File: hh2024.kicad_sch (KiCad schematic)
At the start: 68 parts, among them J1 SAO, J2 QWIIC, J3 Micro_SD_Card, J4 USB-C, K1 SANYOU_SRD_Form_C, Q3 AP2302B, SW1 Multi-Directional-Switches, SW2 Multi-Directional-Switches, SW3 Multi-Directional-Switches, SW4 Multi-Directional-Switches, SW5 Multi-Directional-Switches, U5 CH32V003F4U6, U6 74LVC1G125

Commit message: Fixed the sao ヽ༼ ツ ༽ﾉ
and some routing
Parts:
- J1: footprint BamboulabFootprints:SAO2 -> BamboulabFootprints:SAO Female THT Labels
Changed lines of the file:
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@@
       (effects (font (size 1.27 1.27)) (justify left))
     )
-    (property "Footprint" "BamboulabFootprints:SAO2" (at 149.86 39.37 0)
+    (property "Footprint" "BamboulabFootprints:SAO Female THT Labels" (at 149.86 39.37 0)
       (effects (font (size 1.27 1.27)) hide)
     )

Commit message: Small fixes and change footprint library for missing libraries
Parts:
- removed TP11, TP12, TP13, TP14, TP15, TP16, TP17: TestPoint, TestPoint:TestPoint_Pad_1.0x1.0mm, symbol Connector:TestPoint
- D10, D11, D12, D13, D14, D15, D16, D17, D18, D19, D20, D21, D22, D23, D24, D5, D6, D7, D8, D9: footprint BamboulabFootprints:XL-1606UOC Side Sticker LED -> hh24:XL-1606UOC Side Sticker LED
- D25: footprint tanoshii:D_SOD-323 -> hh24:D_SOD-323
- D26: footprint BamboulabFootprints:SK6805-EC3210R -> hh24:SK6805-EC3210R
- F1: footprint tanoshii:Fuse_0805_2012Metric -> hh24:Fuse_0805_2012Metric
- J1: footprint BamboulabFootprints:SAO Female THT Labels -> hh24:SAO Female THT Labels
- J2: footprint BamboulabFootprints:Qwiic 1X04_1MM_RA_GND -> hh24:Qwiic 1X04_1MM_RA_GND
- J3: footprint tanoshii:MicroSD-SOFNG-TF-002-H18 -> hh24:MicroSD-SOFNG-TF-002-H18
- J4: footprint tanoshii:USB_C_Receptacle_HRO_TYPE-C-31-M-12 -> hh24:USB_C_Receptacle_HRO_TYPE-C-31-M-12
- K1: footprint BamboulabFootprints:HRS1H-S-DC3V -> hh24:HRS1H-S-DC3V
- Q3: footprint tanoshii:SOT-23 -> hh24:SOT-23
- R43: value 10k -> 2.2k; LCSC C5140188 -> (none); Link https://www.lcsc.com/product-detail/Chip-span-style-backgro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 -> (none)
- SW1, SW2, SW3, SW4, SW5: footprint BamboulabFootprints:TM-2023 -> hh24:TM-2023
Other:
- company: Nicolai Electronics x tilde.industries -> Nicolai Electronics & tilde.industries

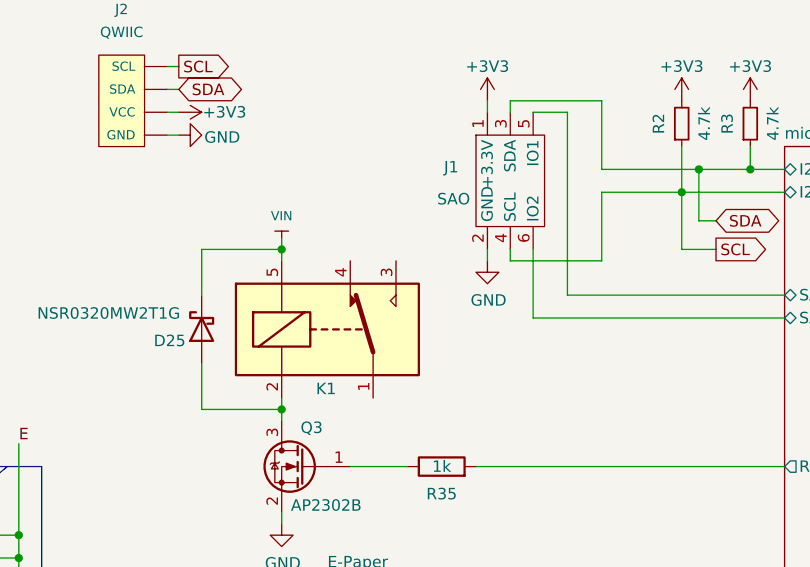
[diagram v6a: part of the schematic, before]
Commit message: Fix power circuit, add headers and move stuff
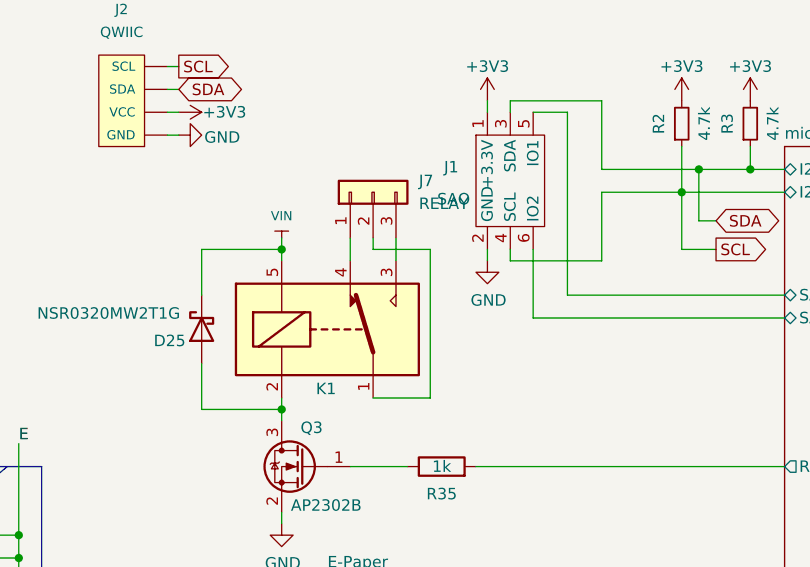
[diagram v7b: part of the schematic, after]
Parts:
- added J7: RELAY, Connector_PinHeader_2.54mm:PinHeader_1x03_P2.54mm_Vertical, symbol Connector_Generic:Conn_01x03
- R1, R28, R29, R30, R34: LCSC C5140188 -> C5140188
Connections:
- net at K1.1: now also J7.2 (Pin_2)
- net at K1.3: now also J7.3 (Pin_3)
- net at K1.4: now also J7.1 (Pin_1)

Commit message: Added art, first pass without DRC
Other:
- note added: "Bottom"
- note added: "Top"
- note removed: "Bottom (Yellow)"
- note removed: "Top (orange)"
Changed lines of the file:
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@@
 		)
 	)
-	(text "Top (orange)"
+	(text "Top\n"
 		(exclude_from_sim no)
 		(at 32.512 69.342 0)
@@
 		)
 	)
-	(text "Bottom (Yellow)"
+	(text "Bottom"
 		(exclude_from_sim no)
 		(at 98.552 124.46 0)
@@
 		(on_board yes)
 		(dnp no)
-		(fields_autoplaced yes)
 		(property "Reference" "J7"
 			(at 139.7 39.3699 90)
@@
 		)
 		(property "Value" "RELAY"
-			(at 139.7 41.9099 90)
+			(at 131.826 38.1 90)
 			(effects
 				(font
